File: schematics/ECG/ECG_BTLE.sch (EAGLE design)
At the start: 31 parts, among them IC1 ADS1293, IC3 MCP1703, IC4 CC2541, U1 ADXL362

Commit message: few changes
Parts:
- added U$5: MICROSD_SD_MODE, con-molex-microsd:MICROSD_SD_MODE
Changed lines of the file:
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@@
 <part name="U$3" library="hirose" deviceset="DF12-3.5-30DP" device=""/>
 <part name="U$4" library="hirose" deviceset="DF12-3.5-30DP" device=""/>
+<part name="U$5" library="con-molex-microsd" deviceset="MICROSD_SD_MODE" device=""/>
 </parts>
 <sheets>
@@
 <instance part="U$3" gate="CONN" x="53.34" y="274.32"/>
 <instance part="U$4" gate="CONN" x="134.62" y="274.32"/>
+<instance part="U$5" gate="G$1" x="45.72" y="185.42"/>
 </instances>
 <busses>

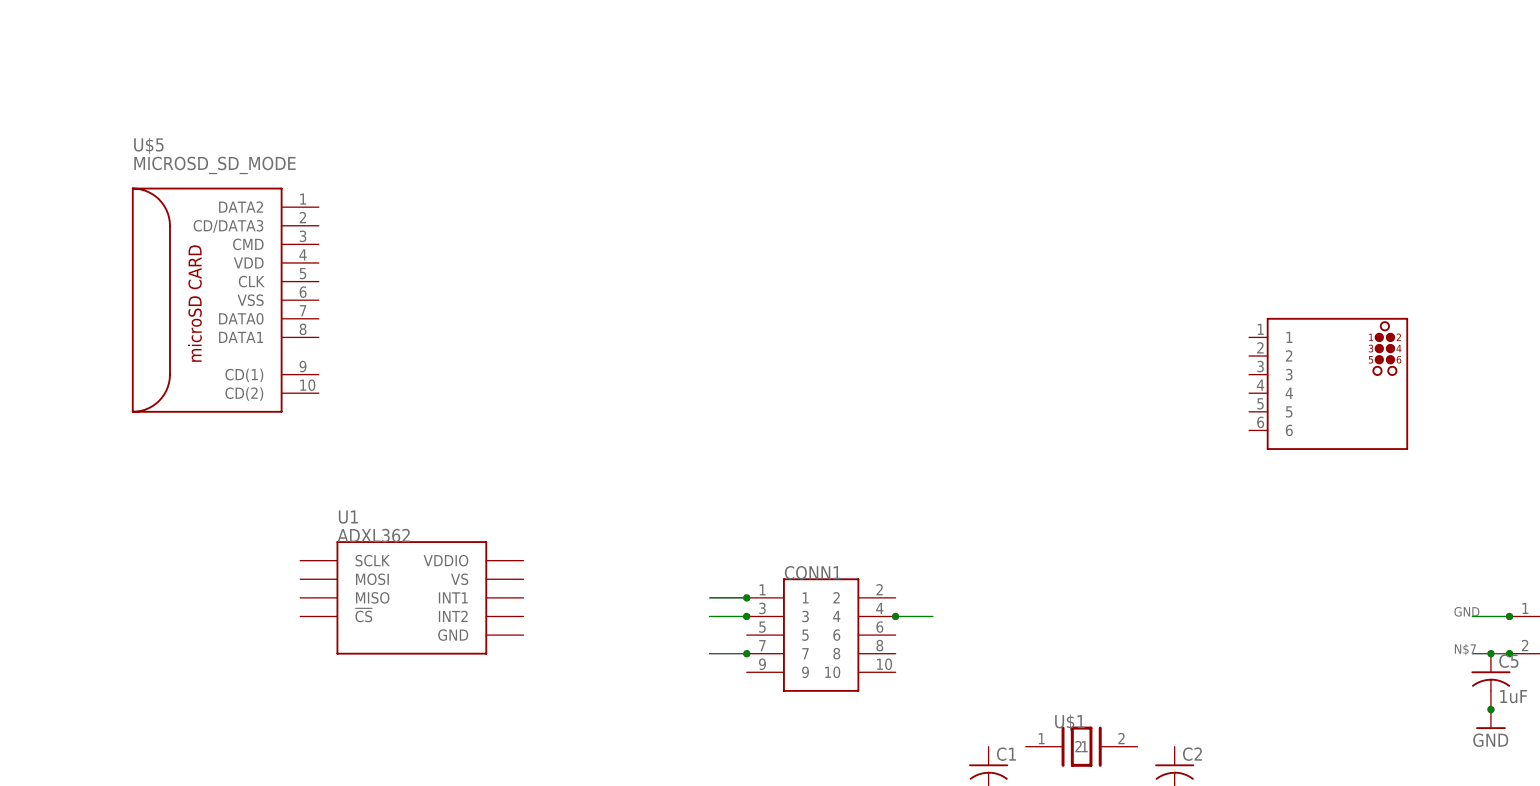
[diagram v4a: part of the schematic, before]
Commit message: removed some unused parts
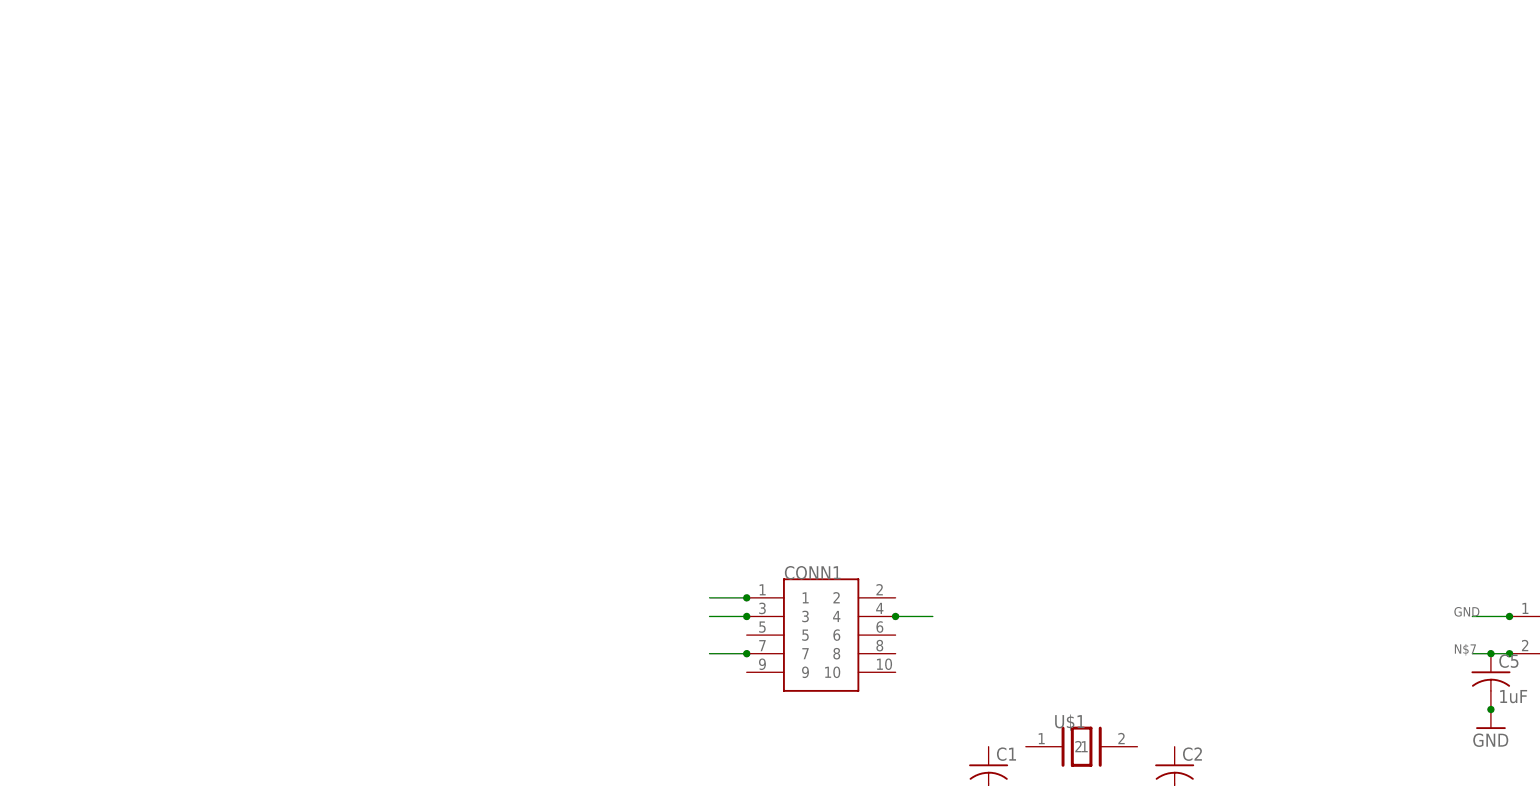
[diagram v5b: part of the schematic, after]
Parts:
- removed U$2: TC2030-MCP-NL, tagconnect:TC2030-MCP-NL
- removed U$5: MICROSD_SD_MODE, con-molex-microsd:MICROSD_SD_MODE
- removed U1: ADXL362, SparkFun-Sensors:ADXL362
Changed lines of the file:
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@@
 <part name="R8" library="rcl" deviceset="R-US_" device="R0201" value="10k"/>
 <part name="R9" library="rcl" deviceset="R-US_" device="R0201" value="10k"/>
-<part name="U1" library="SparkFun-Sensors" deviceset="ADXL362" device="" value="ADXL362"/>
-<part name="U$2" library="tagconnect" deviceset="TC2030" device="-MCP-NL"/>
 <part name="U$3" library="hirose" deviceset="DF12-3.5-30DP" device=""/>
 <part name="U$4" library="hirose" deviceset="DF12-3.5-30DP" device=""/>
-<part name="U$5" library="con-molex-microsd" deviceset="MICROSD_SD_MODE" device=""/>
 </parts>
 <sheets>
@@
 <instance part="R8" gate="G$1" x="396.24" y="99.06" rot="R180"/>
 <instance part="R9" gate="G$1" x="396.24" y="91.44" rot="R180"/>
-<instance part="U1" gate="G$1" x="71.12" y="144.78"/>
-<instance part="U$2" gate="G$1" x="198.12" y="172.72"/>
 <instance part="U$3" gate="CONN" x="53.34" y="274.32"/>
 <instance part="U$4" gate="CONN" x="134.62" y="274.32"/>
-<instance part="U$5" gate="G$1" x="45.72" y="185.42"/>
 </instances>
 <busses>

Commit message: updated board, added BOM template
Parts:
- added C10: 1uF, rcl:C-EUC0402
- added C11: 10uF, rcl:C-EUC0402
- added C14, C15: 12pF, rcl:C-USC0201
- added C16, C17: 10pF, rcl:C-USC0201
- added C9: 0.1uF, rcl:C-EUC0402
- added R10, R11: 1M, resistor:R-US_R0402
- added R12: 0, resistor:R-US_R0402
- added R13, R14: 100K, rcl:R-US_R0201
- added R15: 0, rcl:R-US_R0201
- added TP10, TP11, TP4, TP5, TP6, TP7, TP8, TP9: TPSTP08SQ, testpad:TPSTP08SQ
- added U$2: LIS3DH, st:LIS3DH
- added X1-X: XTAL-2SMD, ecs:XTAL-2SMD
- added X2: XTAL_403, cts:XTAL_403
- C1, C2: value (none) -> 22pF
- C3: value 1nF (01016D102KAT2A) -> 1.5nF
- R5: value 10M (RK73H1HTTC1005F) -> 1M
- R6: value 10K (RK73B1FTTBL103J) -> 100K
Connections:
- removed net 16XCLK: IC4.P1_3
- removed net GATE_R: IC4.P0_5
- removed net GATE_T: IC4.P0_4
- removed net IR_SD: IC4.P0_0
- removed net MCP_RST: IC4.P0_1
- removed net MCU_UART_RX: IC4.P0_2
- removed net MCU_UART_TX: IC4.P0_3
- removed net N$3: CONN1.7
- removed net N$4: CONN1.1
- removed net N$7: C5.1, IC3.VOUT
- removed net P0_6: IC4.P0_6
- removed net P0_7: IC4.P0_7
- removed net VCC_CONTROL: IC4.P1_0
- removed net VDD: C7.1, C8.1, IC1.VDD, IC1.VDDIO
- new net ACCEL_INT1: IC4.P0_7, U$2.INT1
- new net ALARMB: IC1.ALARMB, IC4.P0_1, TP10.PP
- new net BATT_SCALED: IC4.P0_6, R13.1, R14.2
- new net DRDYB: IC1.DRDYB, IC4.P0_0, TP5.PP
- new net IN3: IC1.IN3, R2.2
- new net LL: R2.1, TP3.PP
- new net N$11: C10.1, IC1.RLDIN, IC1.RLDREF
- new net N$12: IC1.SYNCB, R11.2
- new net N$13: U$2.VDDIO
- new net N$5: IC1.RSTB, R10.1
- new net SPI_CSB: IC1.CSB, IC4.P0_4, TP9.PP, U$2.CS
- new net SPI_SCLK: IC1.SCLK, IC4.P0_5, TP8.PP, U$2.SCL/SPC
- new net SPI_SDI: IC1.SDI, IC4.P0_2, TP7.PP, U$2.SDA/SDI
- new net SPI_SDO: IC1.SDO, IC4.P0_3, TP6.PP, U$2.SA0/SDO
- new net XTAL1: C2.2, IC1.XTAL1, U$1.2
- new net XTAL2: C1.2, IC1.XTAL2, U$1.1
- net BATT+: now also R13.2
- net GND: now also C10.2, C11.2, C14.2, C15.2, C16.2, C17.2, C9.2, CONN1.1, R14.1, U$2.GND@10, U$2.GND@12, U$2.GND@5
- net IN2: now also R12.2; no longer R2.2
- net LA: now also R12.1; no longer R2.1
- net N$1: now also CONN1.9, R15.1; no longer CONN1.4
- net N$2: now also R15.2, TP11.PP; no longer CONN1.3
- net P2_1/DD: now also CONN1.4
- net P2_2/DC: now also CONN1.3
- net P2_3/32K_Q2: now also C14.1, X1-X.1
- net P2_4/32K_Q1: now also C15.1, X1-X.2
- net RESET_N: now also CONN1.7
- net RL: now also TP4.PP; no longer TP3.PP
- net VCC: now also C1.1, C11.1, C2.1, C5.1, C7.1, C8.1, C9.1, CONN1.2, IC1.VDD, IC1.VDDIO, IC3.VOUT, R10.2, R11.1, U$2.VDD
- net XOSC_Q1: now also C16.1, X2.1
- net XOSC_Q2: now also C17.1, X2.2
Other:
- note added: "32.768KHz"
- note added: "32MHz"
- note added: "OPT."
- moved on the sheet: C1, C13, C18, C2, C3, C4, C5, CONN1, IC1, IC3, IC4, R1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
